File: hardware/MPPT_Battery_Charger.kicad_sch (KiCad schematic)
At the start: 74 parts, among them Q24 SI7414DN-T1-E3, Q25 SI7414DN-T1-E3, Q5 SI2302DDS-T1-GE3, Q5 SI7414DN-T1-E3, Q6 SI7414DN-T1-E3, U22 BQ24650RVAT, U26 LMV321RIYLT, U28 LMV321RIYLT, U4 INA199C1DCKR

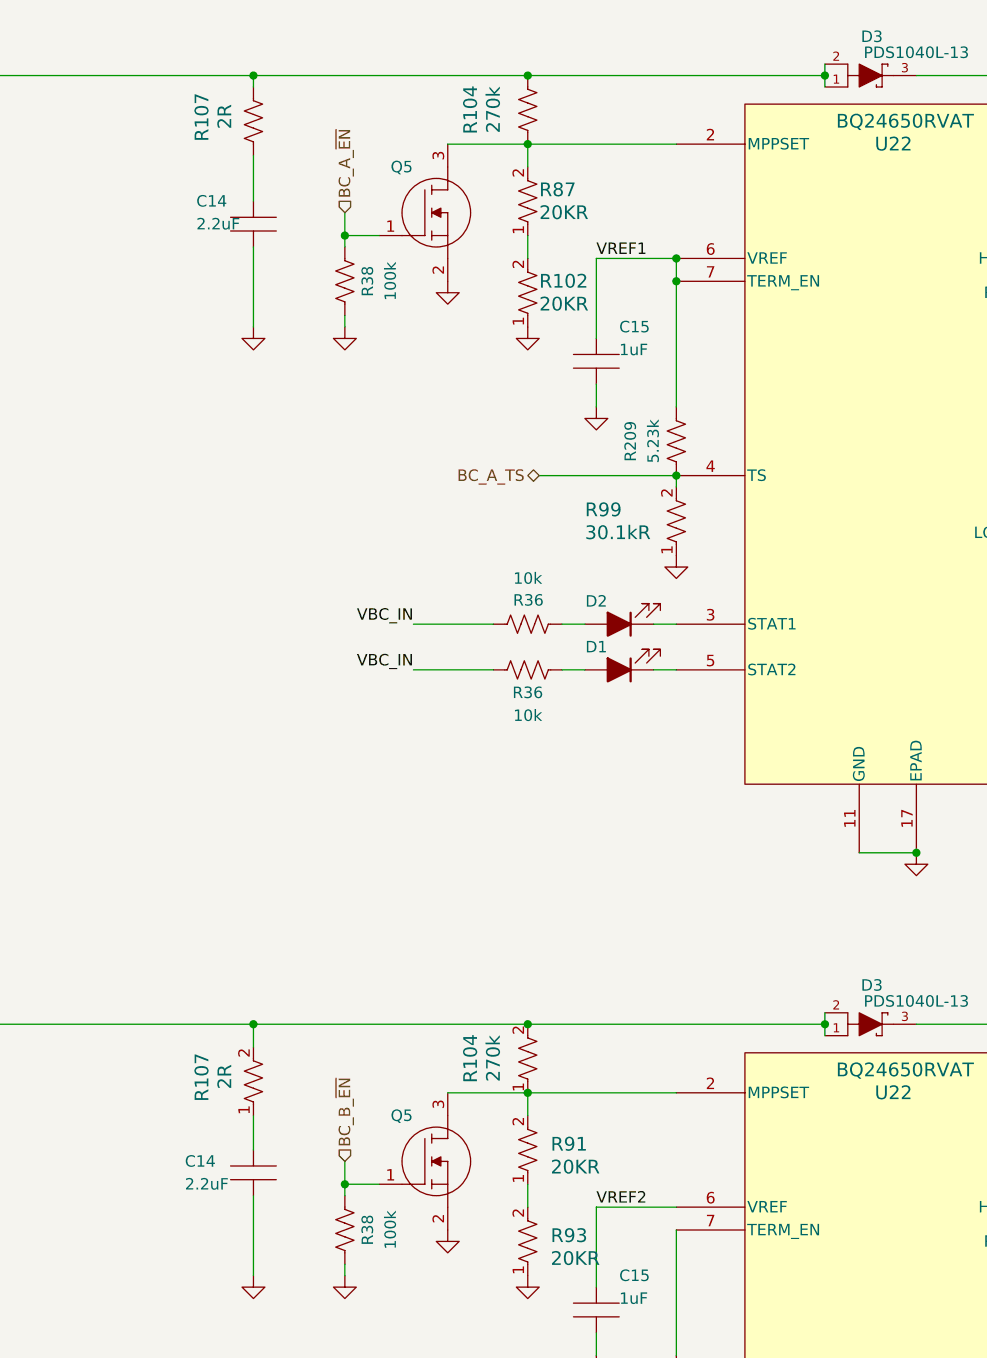
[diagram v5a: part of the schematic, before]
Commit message: hardware: update on footprints
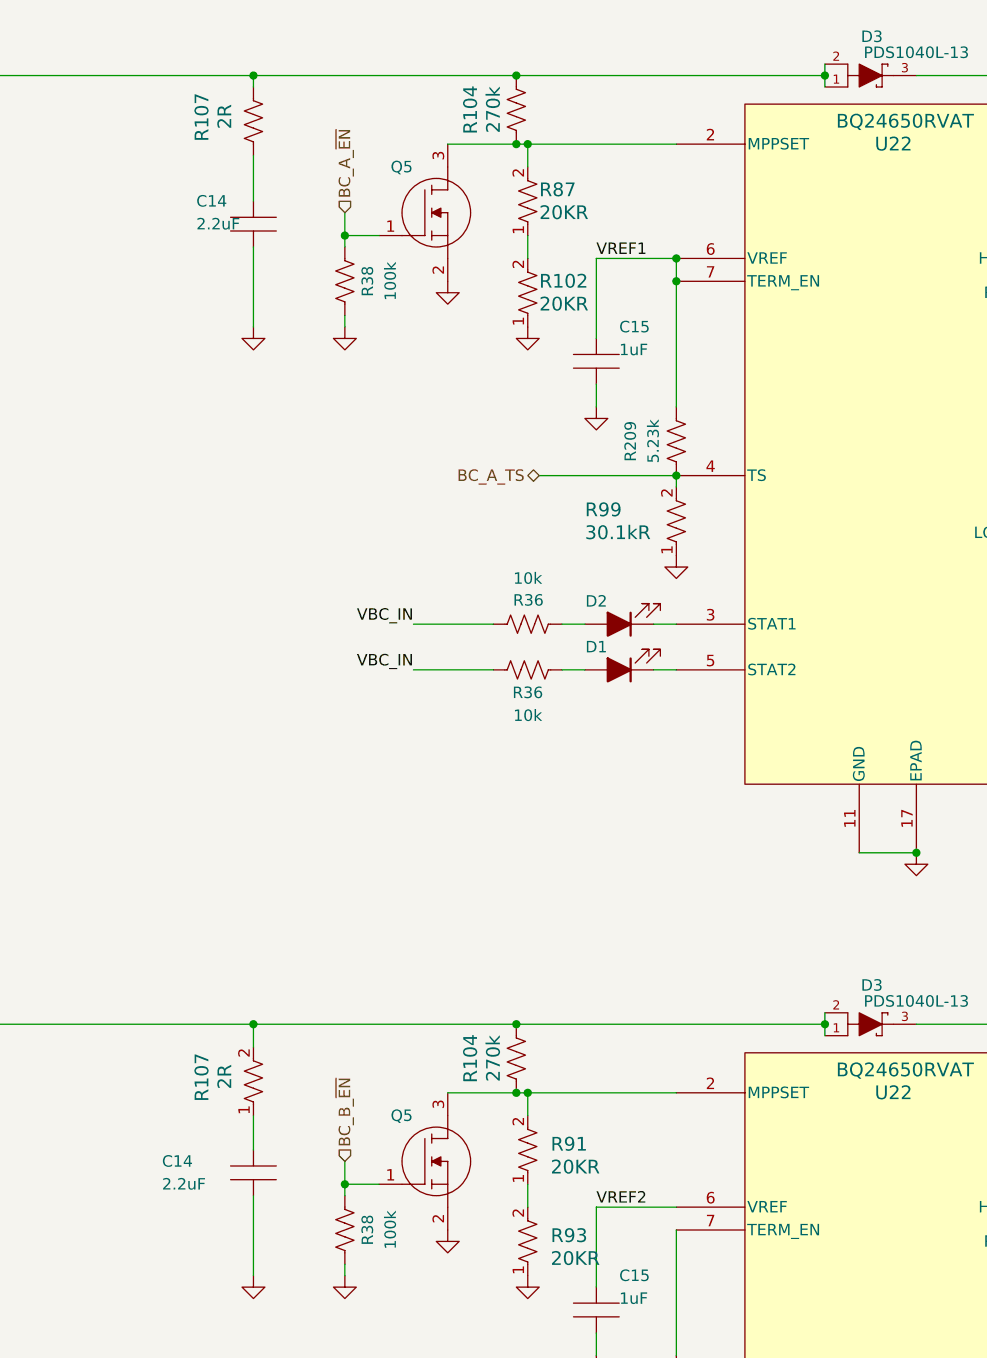
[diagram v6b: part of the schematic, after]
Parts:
- R104: footprint RES_CRCW_0805_VIS -> footprints:CRCW0805270KFKEAHP; symbol CRCW0805270KFKEAHP:CRCW080520K0FKEAHP -> CRCW0805270KFKEAHP:CRCW0805270KFKEAHP
- R104: symbol CRCW0805270KFKEAHP:CRCW080520K0FKEAHP -> CRCW0805270KFKEAHP:CRCW0805270KFKEAHP
- R87: footprint RES_CRCW_0805_VIS -> footprints:CRCW080520K0FKEAHP
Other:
- moved on the sheet: R104
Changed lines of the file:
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@@
   (junction (at 196.85 161.29) (diameter 0) (color 0 0 0 0)
   )
+  (junction (at 132.08 31.75) (diameter 0) (color 0 0 0 0)
+  )
   (junction (at 196.85 48.26) (diameter 0) (color 0 0 0 0)
   )
@@
   (junction (at 312.42 60.96) (diameter 0) (color 0 0 0 0)
   )
-  (junction (at 133.35 24.13) (diameter 0) (color 0 0 0 0)
-  )
   (junction (at 113.03 147.32) (diameter 0) (color 0 0 0 0)
   )
@@
   (junction (at 166.37 24.13) (diameter 0) (color 0 0 0 0)
   )
+  (junction (at 132.08 24.13) (diameter 0) (color 0 0 0 0)
+  )
   (junction (at 196.85 168.91) (diameter 0) (color 0 0 0 0)
   )
+  (junction (at 132.08 129.54) (diameter 0) (color 0 0 0 0)
+  )
   (junction (at 223.52 129.54) (diameter 0) (color 0 0 0 0)
   )
@@
   (junction (at 196.85 31.75) (diameter 0) (color 0 0 0 0)
   )
+  (junction (at 132.08 137.16) (diameter 0) (color 0 0 0 0)
+  )
   (junction (at 262.89 24.13) (diameter 0) (color 0 0 0 0)
   )
@@
   (junction (at 360.68 74.93) (diameter 0) (color 0 0 0 0)
   )
-  (junction (at 133.35 129.54) (diameter 0) (color 0 0 0 0)
-  )
   (junction (at 256.54 165.1) (diameter 0) (color 0 0 0 0)
   )
@@
     (stroke (width 0) (type default))
   )
-  (wire (pts (xy 102.87 24.13) (xy 133.35 24.13))
+  (wire (pts (xy 102.87 24.13) (xy 132.08 24.13))
     (stroke (width 0) (type default))
   )
@@
     (stroke (width 0) (type default))
   )
+  (wire (pts (xy 133.35 31.75) (xy 149.86 31.75))
+    (stroke (width 0) (type default))
+  )
   (wire (pts (xy 100.33 223.52) (xy 100.33 231.14))
     (stroke (width 0) (type default))
@@
     (stroke (width 0) (type default))
   )
-  (wire (pts (xy 102.87 129.54) (xy 133.35 129.54))
+  (wire (pts (xy 45.72 24.13) (xy 52.07 24.13))
     (stroke (width 0) (type default))
   )
-  (wire (pts (xy 45.72 24.13) (xy 52.07 24.13))
+  (wire (pts (xy 132.08 137.16) (xy 133.35 137.16))
     (stroke (width 0) (type default))
   )
@@
     (stroke (width 0) (type default))
   )
+  (wire (pts (xy 132.08 129.54) (xy 166.37 129.54))
+    (stroke (width 0) (type default))
+  )
   (wire (pts (xy 369.57 87.63) (xy 379.73 87.63))
     (stroke (width 0) (type default))
@@
     (stroke (width 0) (type default))
   )
-  (wire (pts (xy 124.46 31.75) (xy 133.35 31.75))
+  (wire (pts (xy 124.46 31.75) (xy 132.08 31.75))
     (stroke (width 0) (type default))
   )
@@
     (stroke (width 0) (type default))
   )
-  (wire (pts (xy 133.35 129.54) (xy 166.37 129.54))
+  (wire (pts (xy 102.87 129.54) (xy 132.08 129.54))
     (stroke (width 0) (type default))
   )
@@
     (stroke (width 0) (type default))
   )
-  (wire (pts (xy 133.35 31.75) (xy 149.86 31.75))
-    (stroke (width 0) (type default))
-  )
   (wire (pts (xy 203.2 161.29) (xy 196.85 161.29))
     (stroke (width 0) (type default))
@@
     (stroke (width 0) (type default))
   )
+  (wire (pts (xy 132.08 24.13) (xy 166.37 24.13))
+    (stroke (width 0) (type default))
+  )
   (wire (pts (xy 358.14 240.03) (xy 358.14 247.65))
     (stroke (width 0) (type default))
@@
     (stroke (width 0) (type default))
   )
+  (wire (pts (xy 132.08 31.75) (xy 133.35 31.75))
+    (stroke (width 0) (type default))
+  )
   (wire (pts (xy 203.2 31.75) (xy 196.85 31.75))
     (stroke (width 0) (type default))
@@
     (stroke (width 0) (type default))
   )
-  (wire (pts (xy 124.46 137.16) (xy 133.35 137.16))
+  (wire (pts (xy 124.46 137.16) (xy 132.08 137.16))
     (stroke (width 0) (type default))
   )
@@
     (stroke (width 0) (type default))
   )
-  (wire (pts (xy 133.35 24.13) (xy 166.37 24.13))
-    (stroke (width 0) (type default))
-  )
   (wire (pts (xy 196.85 60.96) (xy 196.85 63.5))
     (stroke (width 0) (type default))
@@
       (effects (font (size 1.524 1.524)) (justify right))
     )
-    (property "Footprint" "RES_CRCW_0805_VIS" (at 132.08 44.45 0)
+    (property "Footprint" "footprints:CRCW080520K0FKEAHP" (at 132.08 44.45 0)
       (effects (font (size 1.27 1.27) italic) hide)
     )
@@
     )
   )
-  (symbol (lib_id "CRCW0805270KFKEAHP:CRCW080520K0FKEAHP") (at 132.08 139.7 90) (unit 1)
+  (symbol (lib_id "CRCW0805270KFKEAHP:CRCW0805270KFKEAHP") (at 132.08 139.7 90) (unit 1)
     (in_bom yes) (on_board yes) (dnp no)
     (property "Reference" "R104" (at 127 133.35 0)
@@
       (effects (font (size 1.524 1.524)))
     )
-    (property "Footprint" "RES_CRCW_0805_VIS" (at 132.08 139.7 0)
+    (property "Footprint" "footprints:CRCW0805270KFKEAHP" (at 134.62 133.35 0)
       (effects (font (size 1.27 1.27) italic) hide)
     )
-    (property "Datasheet" "CRCW0805270KFKEAHP" (at 132.08 139.7 0)
+    (property "Datasheet" "CRCW080520K0FKEAHP" (at 137.16 134.62 0)
       (effects (font (size 1.27 1.27) italic) hide)
     )
@@
   (symbol (lib_id "C1210C225K5RACTU:C1210C225K5RACTU") (at 102.87 143.51 0) (unit 1)
     (in_bom yes) (on_board yes) (dnp no)
-    (property "Reference" "C14" (at 95.25 144.78 0)
+    (property "Reference" "C14" (at 92.71 144.78 0)
       (effects (font (size 1.27 1.27)) (justify left))
     )
-    (property "Value" "2.2uF" (at 95.25 147.32 0)
+    (property "Value" "2.2uF" (at 92.71 147.32 0)
       (effects (font (size 1.27 1.27)) (justify left))
     )
@@
     )
   )
-  (symbol (lib_name "CRCW080520K0FKEAHP_1") (lib_id "CRCW0805270KFKEAHP:CRCW080520K0FKEAHP") (at 132.08 34.29 90) (unit 1)
+  (symbol (lib_name "CRCW0805270KFKEAHP_1") (lib_id "CRCW0805270KFKEAHP:CRCW0805270KFKEAHP") (at 132.08 34.29 90) (unit 1)
     (in_bom yes) (on_board yes) (dnp no)
     (property "Reference" "R104" (at 127 27.94 0)
@@
       (effects (font (size 1.524 1.524)))
     )
-    (property "Footprint" "footprints:CRCW0805270KFKEAHP" (at 132.08 34.29 0)
+    (property "Footprint" "footprints:CRCW0805270KFKEAHP" (at 134.62 27.94 0)
       (effects (font (size 1.27 1.27) italic) hide)
     )
-    (property "Datasheet" "CRCW0805270KFKEAHP" (at 132.08 34.29 0)
+    (property "Datasheet" "CRCW080520K0FKEAHP" (at 137.16 29.21 0)
       (effects (font (size 1.27 1.27) italic) hide)
     )

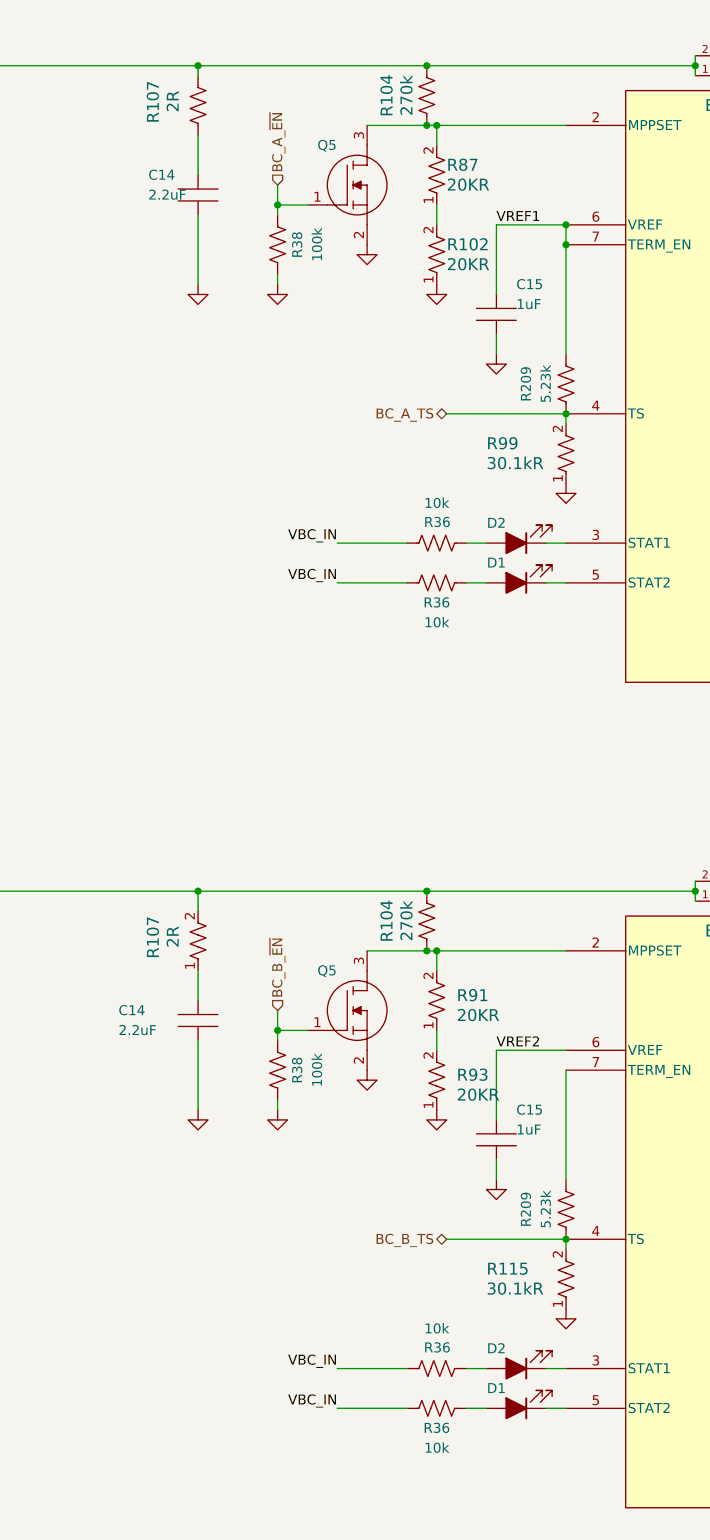
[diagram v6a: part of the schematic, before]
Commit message: hardware: all the resistors were validated, it is only missing the footprint and symbol of one MOSFET and other 4 components which i coulnd't found in the original project.
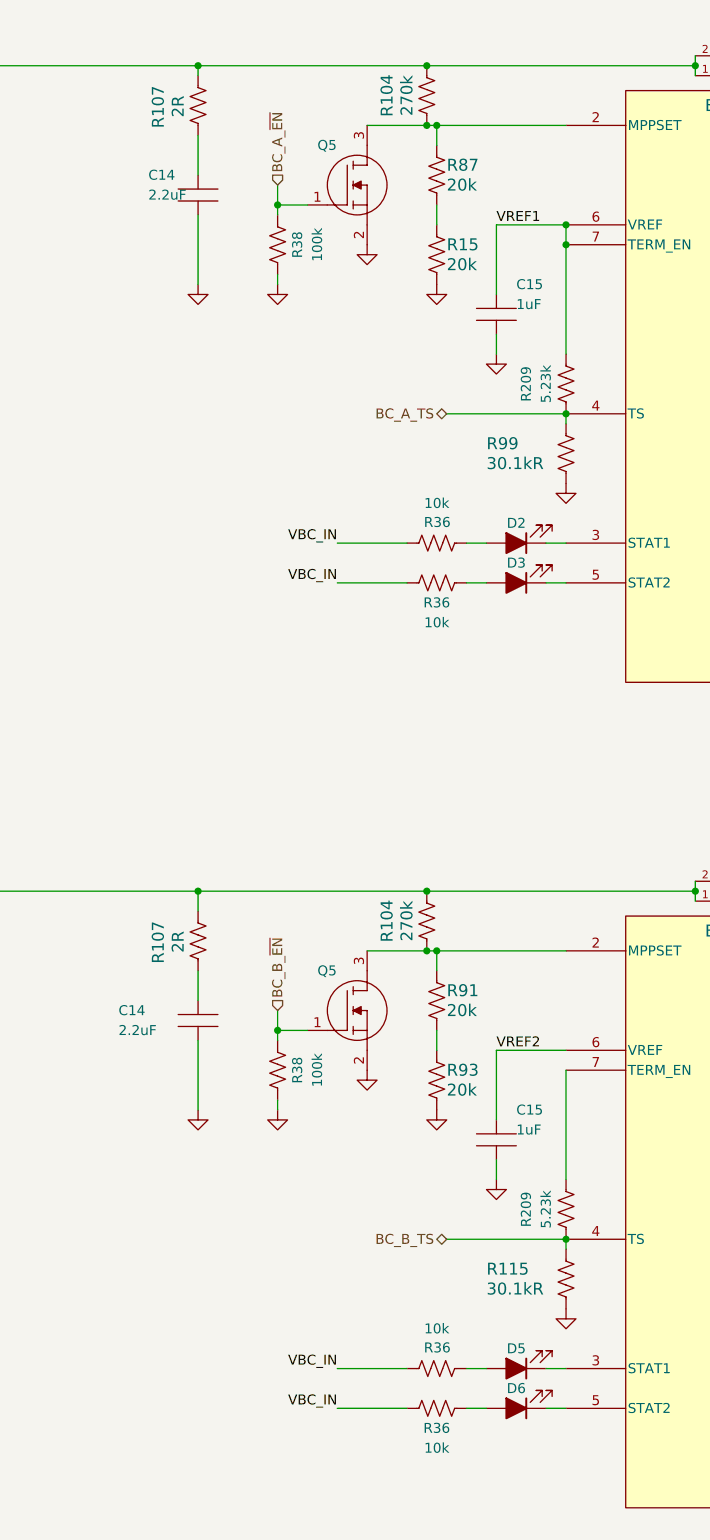
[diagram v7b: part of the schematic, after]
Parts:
- removed D1 (x2), D2 (x2): LED, symbol Device:LED_Filled
- removed R102: 20KR, RES_CRCW_0805_VIS, symbol CRCW080520K0FKEAHP:CRCW080520K0FKEAHP
- added D2, D3, D5, D6: LTST-C190GKT, footprints:LTST-C190GKT, symbol LTST-C190GKT:LTST-C190GKT
- added R15: 20k, footprints:CRCW080520K0FKEAHP, symbol CRCW080520K0FKEAHP:CRCW080520K0FKEAHP
- R107: footprint RC2010N_VIS -> footprints:CRCW20102R00FKEF
- R207: footprint footprints:WSL2512R0330FEA18 -> footprints:WSL2010R0330FEA; symbol WSL2512R0330FEA18:RES -> WSL2010R0330FEA:WSL2010R0330FEA
- R87: value 20KR -> 20k
- R91, R93: value 20KR -> 20k; footprint RES_CRCW_0805_VIS -> footprints:CRCW080520K0FKEAHP
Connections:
- net GND: now also R15.1
- net at R36.2: now also D5.2
- net at U22.5 (STAT2): now also D3.1
- net at R36.2: now also D3.2
- net at R87.1: now also R15.2
- net at U22.3 (STAT1): now also D2.1
- net at R36.2: now also D2.2
- net at U22.3 (STAT1): now also D5.1
- net at U22.5 (STAT2): now also D6.1
- net at R36.2: now also D6.2
